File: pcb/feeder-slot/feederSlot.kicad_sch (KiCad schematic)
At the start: 6 parts, among them J2 Conn_01x05_Female, J3 Conn_01x04_Pin, U1 DS28E07

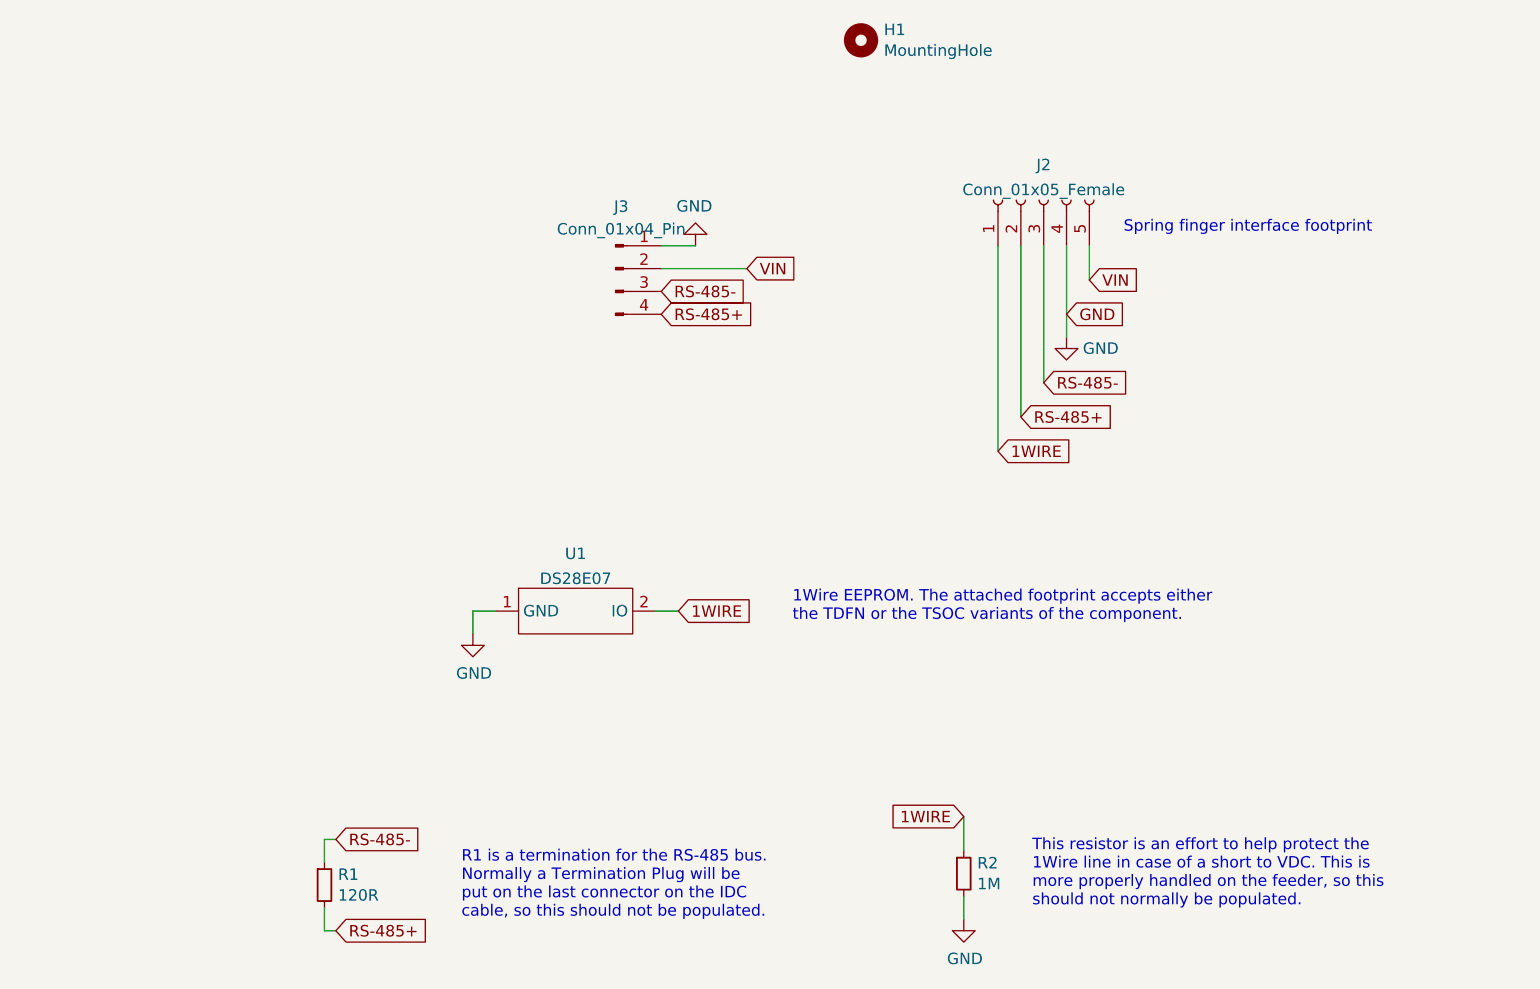
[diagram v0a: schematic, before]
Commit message: updates placement for silk on feeder-slot
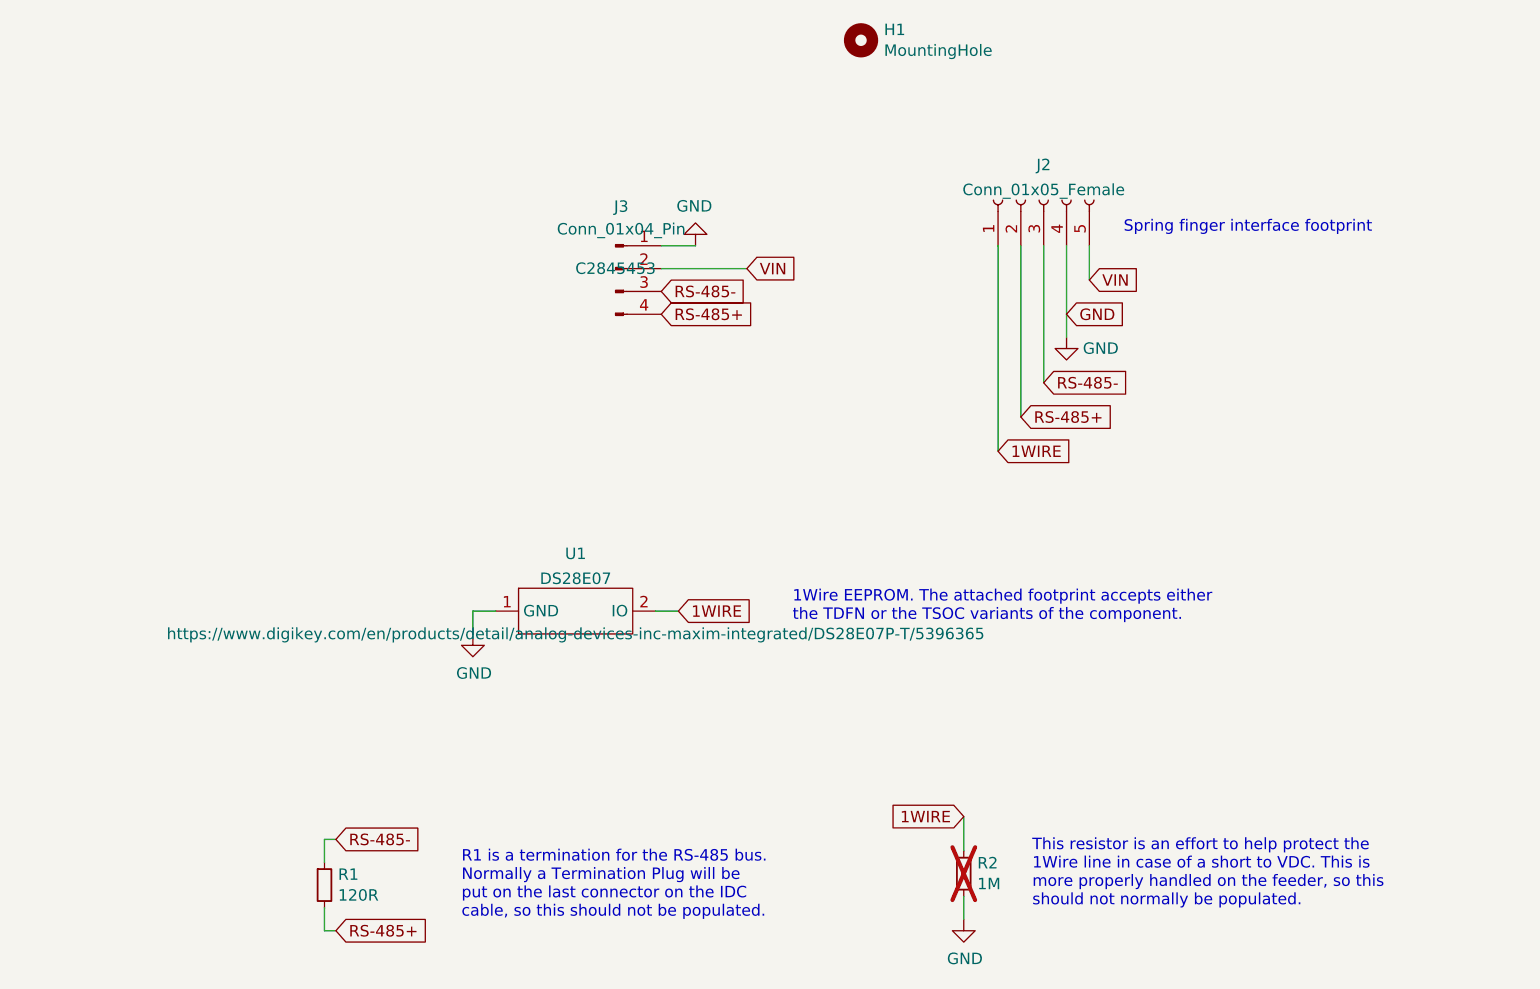
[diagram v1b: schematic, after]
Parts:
- J3: LCSC (none) -> C2845453
- R2: now not fitted; now left out of the parts list
- U1: LCSC (none) -> https://www.digikey.com/en/products/detail/analog-devices-i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
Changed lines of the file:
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@@
+			)
+		)
+		(property "LCSC" "https://www.digikey.com/en/products/detail/analog-devices-inc-maxim-integrated/DS28E07P-T/5396365"
+			(at 125.73 106.68 0)
+			(effects
+				(font
+					(size 1.27 1.27)
+				)
 			)
 		)
@@
 		(unit 1)
 		(exclude_from_sim no)
-		(in_bom yes)
-		(on_board yes)
-		(dnp no)
+		(in_bom no)
+		(on_board no)
+		(dnp yes)
 		(property "Reference" "R2"
 			(at 170.4086 132.1816 0)
@@
 			)
 		)
+		(property "LCSC" "C2845453"
+			(at 130.175 66.04 0)
+			(effects
+				(font
+					(size 1.27 1.27)
+				)
+			)
+		)
